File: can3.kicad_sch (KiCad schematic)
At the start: 7 parts, among them U1 TJA1042T-3

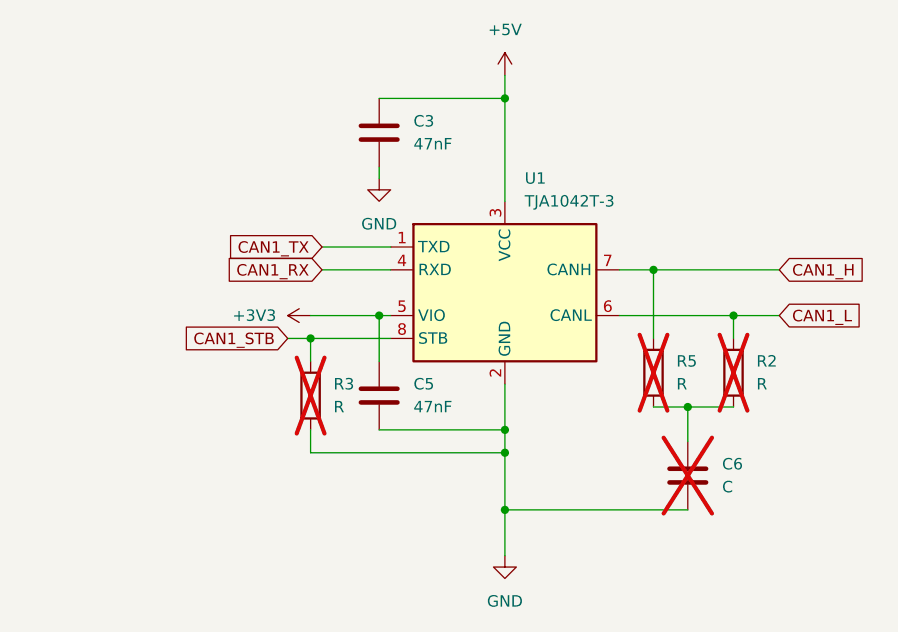
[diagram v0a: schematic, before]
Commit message: add CAN2 and CAN3
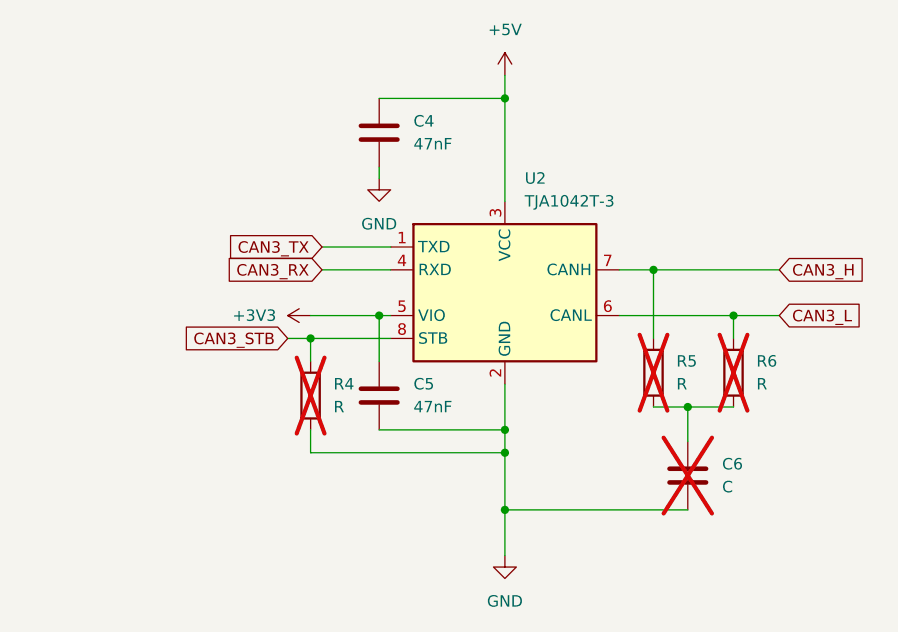
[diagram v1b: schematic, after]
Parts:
- renumbered C3 to C4, R3 to R4, R2 to R6, U1 to U2
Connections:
- net CAN1_H renamed CAN3_H
- net CAN1_L renamed CAN3_L
- net CAN1_RX renamed CAN3_RX
- net CAN1_STB renamed CAN3_STB
- net CAN1_TX renamed CAN3_TX
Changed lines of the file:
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@@
 		)
 	)
-	(global_label "CAN1_H"
+	(global_label "CAN3_H"
 		(shape input)
 		(at 156.21 80.01 0)
@@
 		)
 	)
-	(global_label "CAN1_L"
+	(global_label "CAN3_L"
 		(shape input)
 		(at 156.21 85.09 0)
@@
 		)
 	)
-	(global_label "CAN1_TX"
+	(global_label "CAN3_TX"
 		(shape input)
 		(at 105.41 77.47 180)
@@
 		)
 	)
-	(global_label "CAN1_STB"
+	(global_label "CAN3_STB"
 		(shape input)
 		(at 101.6 87.63 180)
@@
 		)
 	)
-	(global_label "CAN1_RX"
+	(global_label "CAN3_RX"
 		(shape input)
 		(at 105.41 80.01 180)
@@
 		(dnp no)
 		(fields_autoplaced yes)
-		(property "Reference" "#PWR015"
+		(property "Reference" "#PWR017"
 			(at 107.95 85.09 0)
 			(effects
@@
 		(instances
 			(project "sample"
-				(path "/b24c09df-2e49-4fc3-a45d-ba0b1ff2d257/a1e1f3d2-08a6-4ef9-b40d-891f90ca343c"
-					(reference "#PWR015")
+				(path "/b24c09df-2e49-4fc3-a45d-ba0b1ff2d257/ecc88370-915d-48f9-8e29-e68ead91d11e"
+					(reference "#PWR017")
+					(unit 1)
+				)
+				(path "/b24c09df-2e49-4fc3-a45d-ba0b1ff2d257/f47ed58f-27f7-4b09-9f1c-00de47ea5151"
+					(reference "#PWR016")
 					(unit 1)
 				)
@@
 		(dnp no)
 		(fields_autoplaced yes)
-		(property "Reference" "#PWR013"
+		(property "Reference" "#PWR020"
 			(at 125.73 118.11 0)
 			(effects
@@
 		(instances
 			(project "sample"
-				(path "/b24c09df-2e49-4fc3-a45d-ba0b1ff2d257/a1e1f3d2-08a6-4ef9-b40d-891f90ca343c"
-					(reference "#PWR013")
+				(path "/b24c09df-2e49-4fc3-a45d-ba0b1ff2d257/ecc88370-915d-48f9-8e29-e68ead91d11e"
+					(reference "#PWR020")
+					(unit 1)
+				)
+				(path "/b24c09df-2e49-4fc3-a45d-ba0b1ff2d257/f47ed58f-27f7-4b09-9f1c-00de47ea5151"
+					(reference "#PWR023")
 					(unit 1)
 				)
@@
 		(dnp yes)
 		(fields_autoplaced yes)
-		(property "Reference" "R2"
+		(property "Reference" "R6"
 			(at 153.67 90.1699 0)
 			(effects
@@
 		(instances
 			(project "sample"
-				(path "/b24c09df-2e49-4fc3-a45d-ba0b1ff2d257/a1e1f3d2-08a6-4ef9-b40d-891f90ca343c"
-					(reference "R2")
+				(path "/b24c09df-2e49-4fc3-a45d-ba0b1ff2d257/ecc88370-915d-48f9-8e29-e68ead91d11e"
+					(reference "R6")
+					(unit 1)
+				)
+				(path "/b24c09df-2e49-4fc3-a45d-ba0b1ff2d257/f47ed58f-27f7-4b09-9f1c-00de47ea5151"
+					(reference "R8")
 					(unit 1)
 				)
@@
 		(pin "1"
 		)
+		(instances
+			(project "sample"
+				(path "/b24c09df-2e49-4fc3-a45d-ba0b1ff2d257/ecc88370-915d-48f9-8e29-e68ead91d11e"
+					(reference "C5")
+					(unit 1)
+				)
+				(path "/b24c09df-2e49-4fc3-a45d-ba0b1ff2d257/f47ed58f-27f7-4b09-9f1c-00de47ea5151"
+					(reference "C2")
+					(unit 1)
+				)
+			)
+		)
 	)
 	(symbol
@@
 		(dnp no)
 		(fields_autoplaced yes)
-		(property "Reference" "U1"
+		(property "Reference" "U2"
 			(at 127.9241 69.85 0)
 			(effects
@@
 		(instances
 			(project "sample"
-				(path "/b24c09df-2e49-4fc3-a45d-ba0b1ff2d257/a1e1f3d2-08a6-4ef9-b40d-891f90ca343c"
-					(reference "U1")
+				(path "/b24c09df-2e49-4fc3-a45d-ba0b1ff2d257/ecc88370-915d-48f9-8e29-e68ead91d11e"
+					(reference "U2")
+					(unit 1)
+				)
+				(path "/b24c09df-2e49-4fc3-a45d-ba0b1ff2d257/f47ed58f-27f7-4b09-9f1c-00de47ea5151"
+					(reference "U3")
 					(unit 1)
 				)
@@
 		(dnp no)
 		(fields_autoplaced yes)
-		(property "Reference" "#PWR014"
+		(property "Reference" "#PWR019"
 			(at 125.73 62.23 0)
 			(effects
@@
 		(instances
 			(project "sample"
-				(path "/b24c09df-2e49-4fc3-a45d-ba0b1ff2d257/a1e1f3d2-08a6-4ef9-b40d-891f90ca343c"
-					(reference "#PWR014")
+				(path "/b24c09df-2e49-4fc3-a45d-ba0b1ff2d257/ecc88370-915d-48f9-8e29-e68ead91d11e"
+					(reference "#PWR019")
+					(unit 1)
+				)
+				(path "/b24c09df-2e49-4fc3-a45d-ba0b1ff2d257/f47ed58f-27f7-4b09-9f1c-00de47ea5151"
+					(reference "#PWR022")
 					(unit 1)
 				)
@@
 		(pin "1"
 		)
+		(instances
+			(project "sample"
+				(path "/b24c09df-2e49-4fc3-a45d-ba0b1ff2d257/ecc88370-915d-48f9-8e29-e68ead91d11e"
+					(reference "R5")
+					(unit 1)
+				)
+				(path "/b24c09df-2e49-4fc3-a45d-ba0b1ff2d257/f47ed58f-27f7-4b09-9f1c-00de47ea5151"
+					(reference "R7")
+					(unit 1)
+				)
+			)
+		)
 	)
 	(symbol
@@
 		(dnp yes)
 		(fields_autoplaced yes)
-		(property "Reference" "R3"
+		(property "Reference" "R4"
 			(at 106.68 92.7099 0)
 			(effects
@@
 		(instances
 			(project "sample"
-				(path "/b24c09df-2e49-4fc3-a45d-ba0b1ff2d257/a1e1f3d2-08a6-4ef9-b40d-891f90ca343c"
-					(reference "R3")
+				(path "/b24c09df-2e49-4fc3-a45d-ba0b1ff2d257/ecc88370-915d-48f9-8e29-e68ead91d11e"
+					(reference "R4")
+					(unit 1)
+				)
+				(path "/b24c09df-2e49-4fc3-a45d-ba0b1ff2d257/f47ed58f-27f7-4b09-9f1c-00de47ea5151"
+					(reference "R1")
 					(unit 1)
 				)
@@
 		(pin "1"
 		)
+		(instances
+			(project "sample"
+				(path "/b24c09df-2e49-4fc3-a45d-ba0b1ff2d257/ecc88370-915d-48f9-8e29-e68ead91d11e"
+					(reference "#PWR018")
+					(unit 1)
+				)
+				(path "/b24c09df-2e49-4fc3-a45d-ba0b1ff2d257/f47ed58f-27f7-4b09-9f1c-00de47ea5151"
+					(reference "#PWR021")
+					(unit 1)
+				)
+			)
+		)
 	)
 	(symbol
@@
 		(dnp no)
 		(fields_autoplaced yes)
-		(property "Reference" "C3"
+		(property "Reference" "C4"
 			(at 115.57 63.4999 0)
 			(effects
@@
 		(instances
 			(project "sample"
-				(path "/b24c09df-2e49-4fc3-a45d-ba0b1ff2d257/a1e1f3d2-08a6-4ef9-b40d-891f90ca343c"
-					(reference "C3")
+				(path "/b24c09df-2e49-4fc3-a45d-ba0b1ff2d257/ecc88370-915d-48f9-8e29-e68ead91d11e"
+					(reference "C4")
+					(unit 1)
+				)
+				(path "/b24c09df-2e49-4fc3-a45d-ba0b1ff2d257/f47ed58f-27f7-4b09-9f1c-00de47ea5151"
+					(reference "C1")
 					(unit 1)
 				)
@@
 		(pin "1"
 		)
-	)
+		(instances
+			(project "sample"
+				(path "/b24c09df-2e49-4fc3-a45d-ba0b1ff2d257/ecc88370-915d-48f9-8e29-e68ead91d11e"
+					(reference "C6")
+					(unit 1)
+				)
+				(path "/b24c09df-2e49-4fc3-a45d-ba0b1ff2d257/f47ed58f-27f7-4b09-9f1c-00de47ea5151"
+					(reference "C7")
+					(unit 1)
+				)
+			)
+		)
+	)

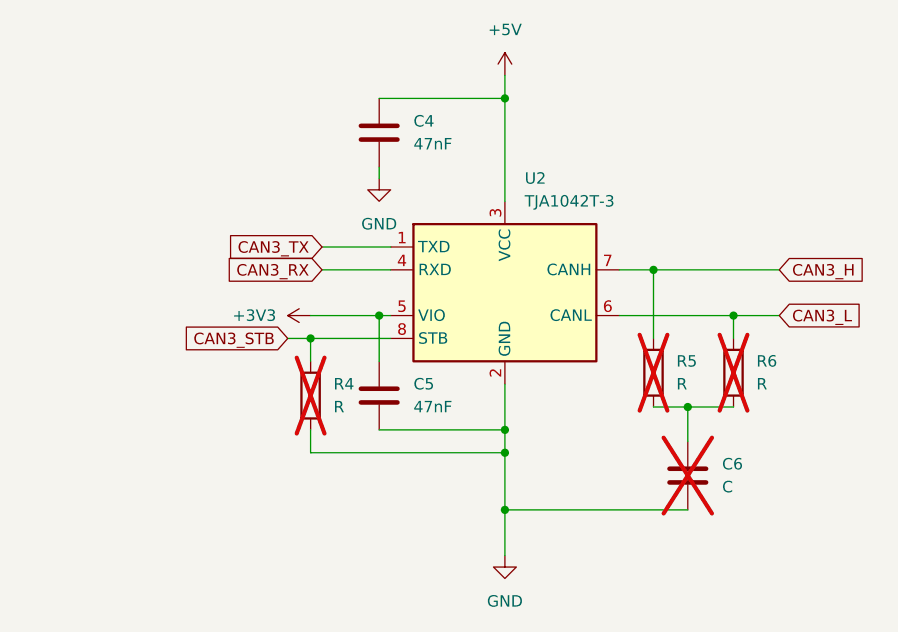
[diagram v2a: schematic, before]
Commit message: add CAN Sub-D connectors
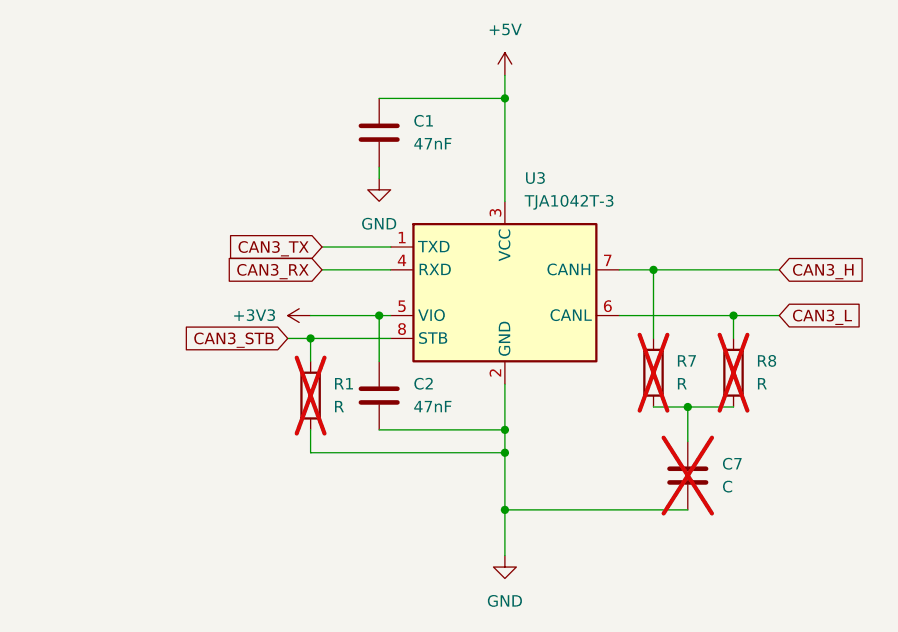
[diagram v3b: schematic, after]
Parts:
- renumbered C4 to C1, C5 to C2, C6 to C7, R4 to R1, R5 to R7, R6 to R8, U2 to U3
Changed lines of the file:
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@@
 		(dnp yes)
 		(fields_autoplaced yes)
-		(property "Reference" "R4"
+		(property "Reference" "R1"
 			(at 106.68 92.7099 0)
 			(effects
@@
 		(instances
 			(project "sample"
-				(path "/b24c09df-2e49-4fc3-a45d-ba0b1ff2d257/ecc88370-915d-48f9-8e29-e68ead91d11e"
-					(reference "R4")
-					(unit 1)
-				)
 				(path "/b24c09df-2e49-4fc3-a45d-ba0b1ff2d257/f47ed58f-27f7-4b09-9f1c-00de47ea5151"
 					(reference "R1")
@@
 		(dnp no)
 		(fields_autoplaced yes)
-		(property "Reference" "#PWR019"
+		(property "Reference" "#PWR022"
 			(at 125.73 62.23 0)
 			(effects
@@
 		(instances
 			(project "sample"
-				(path "/b24c09df-2e49-4fc3-a45d-ba0b1ff2d257/ecc88370-915d-48f9-8e29-e68ead91d11e"
-					(reference "#PWR019")
-					(unit 1)
-				)
 				(path "/b24c09df-2e49-4fc3-a45d-ba0b1ff2d257/f47ed58f-27f7-4b09-9f1c-00de47ea5151"
 					(reference "#PWR022")
@@
 		(dnp no)
 		(fields_autoplaced yes)
-		(property "Reference" "C5"
+		(property "Reference" "C2"
 			(at 115.57 92.7099 0)
 			(effects
@@
 		(instances
 			(project "sample"
-				(path "/b24c09df-2e49-4fc3-a45d-ba0b1ff2d257/ecc88370-915d-48f9-8e29-e68ead91d11e"
-					(reference "C5")
-					(unit 1)
-				)
 				(path "/b24c09df-2e49-4fc3-a45d-ba0b1ff2d257/f47ed58f-27f7-4b09-9f1c-00de47ea5151"
 					(reference "C2")
@@
 		(dnp no)
 		(fields_autoplaced yes)
-		(property "Reference" "U2"
+		(property "Reference" "U3"
 			(at 127.9241 69.85 0)
 			(effects
@@
 		(instances
 			(project "sample"
-				(path "/b24c09df-2e49-4fc3-a45d-ba0b1ff2d257/ecc88370-915d-48f9-8e29-e68ead91d11e"
-					(reference "U2")
-					(unit 1)
-				)
 				(path "/b24c09df-2e49-4fc3-a45d-ba0b1ff2d257/f47ed58f-27f7-4b09-9f1c-00de47ea5151"
 					(reference "U3")
@@
 		(dnp yes)
 		(fields_autoplaced yes)
-		(property "Reference" "C6"
+		(property "Reference" "C7"
 			(at 149.86 101.5999 0)
 			(effects
@@
 		(instances
 			(project "sample"
-				(path "/b24c09df-2e49-4fc3-a45d-ba0b1ff2d257/ecc88370-915d-48f9-8e29-e68ead91d11e"
-					(reference "C6")
-					(unit 1)
-				)
 				(path "/b24c09df-2e49-4fc3-a45d-ba0b1ff2d257/f47ed58f-27f7-4b09-9f1c-00de47ea5151"
 					(reference "C7")
@@
 		(dnp no)
 		(fields_autoplaced yes)
-		(property "Reference" "#PWR020"
+		(property "Reference" "#PWR023"
 			(at 125.73 118.11 0)
 			(effects
@@
 		(instances
 			(project "sample"
-				(path "/b24c09df-2e49-4fc3-a45d-ba0b1ff2d257/ecc88370-915d-48f9-8e29-e68ead91d11e"
-					(reference "#PWR020")
-					(unit 1)
-				)
 				(path "/b24c09df-2e49-4fc3-a45d-ba0b1ff2d257/f47ed58f-27f7-4b09-9f1c-00de47ea5151"
 					(reference "#PWR023")
@@
 		(dnp no)
 		(fields_autoplaced yes)
-		(property "Reference" "C4"
+		(property "Reference" "C1"
 			(at 115.57 63.4999 0)
 			(effects
@@
 		(instances
 			(project "sample"
-				(path "/b24c09df-2e49-4fc3-a45d-ba0b1ff2d257/ecc88370-915d-48f9-8e29-e68ead91d11e"
-					(reference "C4")
-					(unit 1)
-				)
 				(path "/b24c09df-2e49-4fc3-a45d-ba0b1ff2d257/f47ed58f-27f7-4b09-9f1c-00de47ea5151"
 					(reference "C1")
@@
 		(dnp no)
 		(fields_autoplaced yes)
-		(property "Reference" "#PWR017"
+		(property "Reference" "#PWR016"
 			(at 107.95 85.09 0)
 			(effects
@@
 		(instances
 			(project "sample"
-				(path "/b24c09df-2e49-4fc3-a45d-ba0b1ff2d257/ecc88370-915d-48f9-8e29-e68ead91d11e"
-					(reference "#PWR017")
-					(unit 1)
-				)
 				(path "/b24c09df-2e49-4fc3-a45d-ba0b1ff2d257/f47ed58f-27f7-4b09-9f1c-00de47ea5151"
 					(reference "#PWR016")
@@
 		(dnp yes)
 		(fields_autoplaced yes)
-		(property "Reference" "R5"
+		(property "Reference" "R7"
 			(at 144.78 90.1699 0)
 			(effects
@@
 		(instances
 			(project "sample"
-				(path "/b24c09df-2e49-4fc3-a45d-ba0b1ff2d257/ecc88370-915d-48f9-8e29-e68ead91d11e"
-					(reference "R5")
-					(unit 1)
-				)
 				(path "/b24c09df-2e49-4fc3-a45d-ba0b1ff2d257/f47ed58f-27f7-4b09-9f1c-00de47ea5151"
 					(reference "R7")
@@
 		(dnp no)
 		(fields_autoplaced yes)
-		(property "Reference" "#PWR018"
+		(property "Reference" "#PWR021"
 			(at 111.76 76.2 0)
 			(effects
@@
 		(instances
 			(project "sample"
-				(path "/b24c09df-2e49-4fc3-a45d-ba0b1ff2d257/ecc88370-915d-48f9-8e29-e68ead91d11e"
-					(reference "#PWR018")
-					(unit 1)
-				)
 				(path "/b24c09df-2e49-4fc3-a45d-ba0b1ff2d257/f47ed58f-27f7-4b09-9f1c-00de47ea5151"
 					(reference "#PWR021")
@@
 		(dnp yes)
 		(fields_autoplaced yes)
-		(property "Reference" "R6"
+		(property "Reference" "R8"
 			(at 153.67 90.1699 0)
 			(effects
@@
 		(instances
 			(project "sample"
-				(path "/b24c09df-2e49-4fc3-a45d-ba0b1ff2d257/ecc88370-915d-48f9-8e29-e68ead91d11e"
-					(reference "R6")
-					(unit 1)
-				)
 				(path "/b24c09df-2e49-4fc3-a45d-ba0b1ff2d257/f47ed58f-27f7-4b09-9f1c-00de47ea5151"
 					(reference "R8")

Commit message: add CAN STB pins
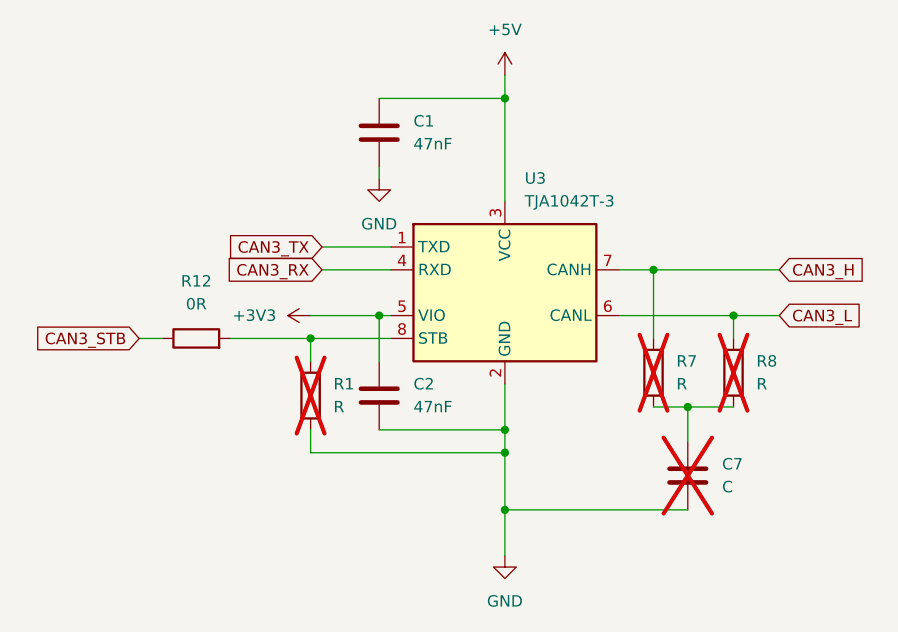
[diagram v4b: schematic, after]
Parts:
- added R12: 0R, Resistor_SMD:R_1206_3216Metric_Pad1.30x1.75mm_HandSolder, symbol Device:R
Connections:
- net CAN3_STB: now also R12.1; no longer R1.1, U3.8 (STB)
- new net: R1.1, R12.2, U3.8 (STB)
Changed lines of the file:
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@@
+	)
+	(junction
+		(at 125.73 106.68)
+		(diameter 0)
+		(color 0 0 0 0)
 	)
 	(junction
@@
 	)
 	(junction
-		(at 125.73 106.68)
-		(diameter 0)
-		(color 0 0 0 0)
-	)
-	(junction
 		(at 151.13 85.09)
 		(diameter 0)
@@
 	(wire
 		(pts
+			(xy 95.25 87.63) (xy 104.14 87.63)
+		)
+		(stroke
+			(width 0)
+			(type default)
+		)
+	)
+	(wire
+		(pts
 			(xy 111.76 97.79) (xy 125.73 97.79)
 		)
@@
 	(wire
 		(pts
+			(xy 85.09 87.63) (xy 87.63 87.63)
+		)
+		(stroke
+			(width 0)
+			(type default)
+		)
+	)
+	(wire
+		(pts
 			(xy 125.73 100.33) (xy 125.73 106.68)
 		)
@@
 		(pts
 			(xy 125.73 60.96) (xy 125.73 72.39)
-		)
-		(stroke
-			(width 0)
-			(type default)
-		)
-	)
-	(wire
-		(pts
-			(xy 101.6 87.63) (xy 104.14 87.63)
 		)
 		(stroke
@@
 	(global_label "CAN3_STB"
 		(shape input)
-		(at 101.6 87.63 180)
+		(at 85.09 87.63 180)
 		(fields_autoplaced yes)
 		(effects
@@
 		)
 		(property "Intersheetrefs" "${INTERSHEET_REFS}"
-			(at 89.3015 87.63 0)
+			(at 72.7915 87.63 0)
 			(effects
 				(font
@@
 					(unit 1)
 				)
+			)
+		)
+	)
+	(symbol
+		(lib_id "Device:R")
+		(at 91.44 87.63 90)
+		(unit 1)
+		(exclude_from_sim no)
+		(in_bom yes)
+		(on_board yes)
+		(dnp no)
+		(fields_autoplaced yes)
+		(property "Reference" "R12"
+			(at 91.44 81.28 90)
+			(effects
+				(font
+					(size 1.27 1.27)
+				)
+			)
+		)
+		(property "Value" "0R"
+			(at 91.44 83.82 90)
+			(effects
+				(font
+					(size 1.27 1.27)
+				)
+			)
+		)
+		(property "Footprint" "Resistor_SMD:R_1206_3216Metric_Pad1.30x1.75mm_HandSolder"
+			(at 91.44 89.408 90)
+			(effects
+				(font
+					(size 1.27 1.27)
+				)
+				(hide yes)
+			)
+		)
+		(property "Datasheet" "~"
+			(at 91.44 87.63 0)
+			(effects
+				(font
+					(size 1.27 1.27)
+				)
+				(hide yes)
+			)
+		)
+		(property "Description" "Resistor"
+			(at 91.44 87.63 0)
+			(effects
+				(font
+					(size 1.27 1.27)
+				)
+				(hide yes)
+			)
+		)
+		(pin "2"
+		)
+		(pin "1"
+		)
+		(instances
+			(project "sample"
+				(path "/b24c09df-2e49-4fc3-a45d-ba0b1ff2d257/f47ed58f-27f7-4b09-9f1c-00de47ea5151"
+					(reference "R12")
+					(unit 1)
+				)
